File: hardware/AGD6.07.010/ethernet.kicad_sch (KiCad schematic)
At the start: 0 parts

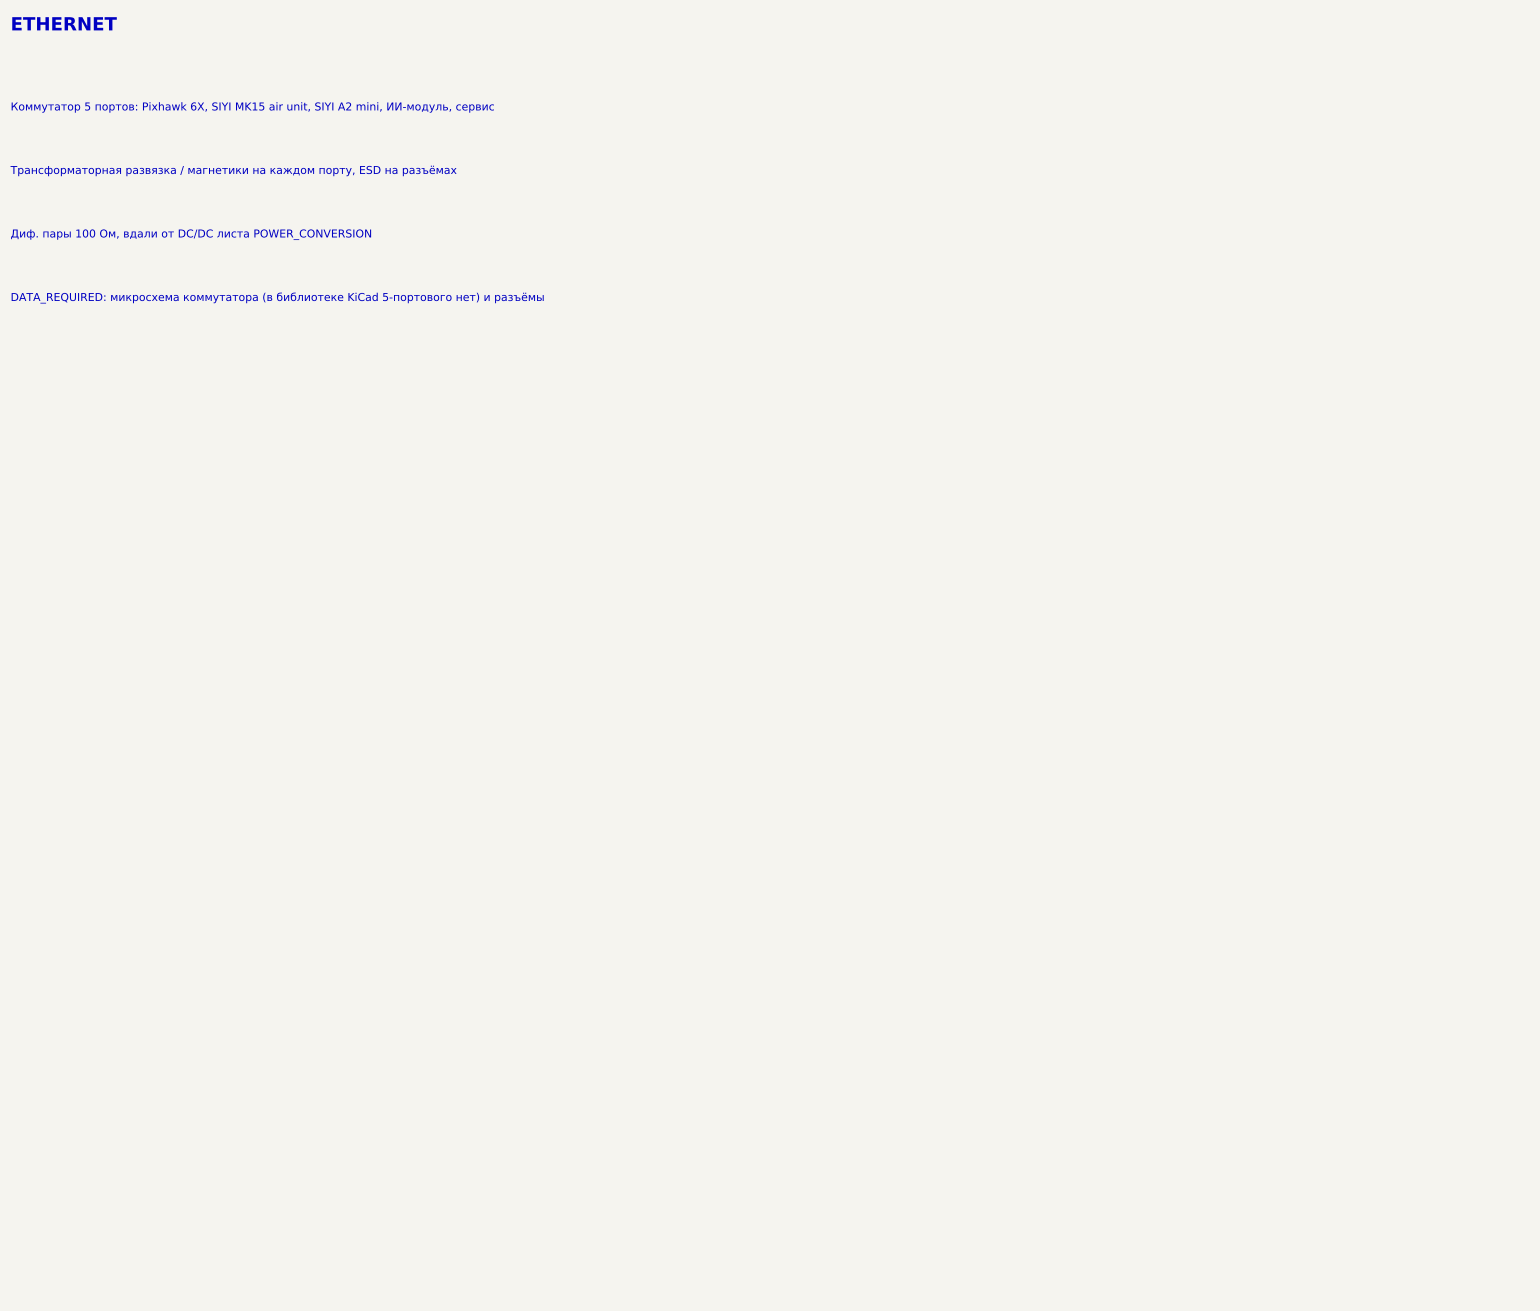
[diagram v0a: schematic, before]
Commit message: Draw full AGD6.07.010 schematic per integrated_avionics_board spec
All ten sheets now carry components: 14S input with hot-swap and power
monitor, 12/5/3.3 V rails and a separate 12 V AI channel with soft-start
and current telemetry, Pixhawk connectors, CAN1/CAN2 hub with chokes,
ESD and switchable termination, sensor conditioning, SIYI and radar,
AI interface and watchdog, protected 12 V switches with diagnostics,
fan/heater control, cameras and Ethernet. Open choices are recorded in
DECISIONS.md; datasheet-dependent values are flagged CHECK_DATASHEET.

ERC: no errors. All 752 intended pin connections match the KiCad netlist.

Co-Authored-By: Claude Opus 5.5 <noreply@anthropic.com>
Claude-Session: https://claude.ai/code/session_01Qk7uTKdi6YbndB9fGuguYV
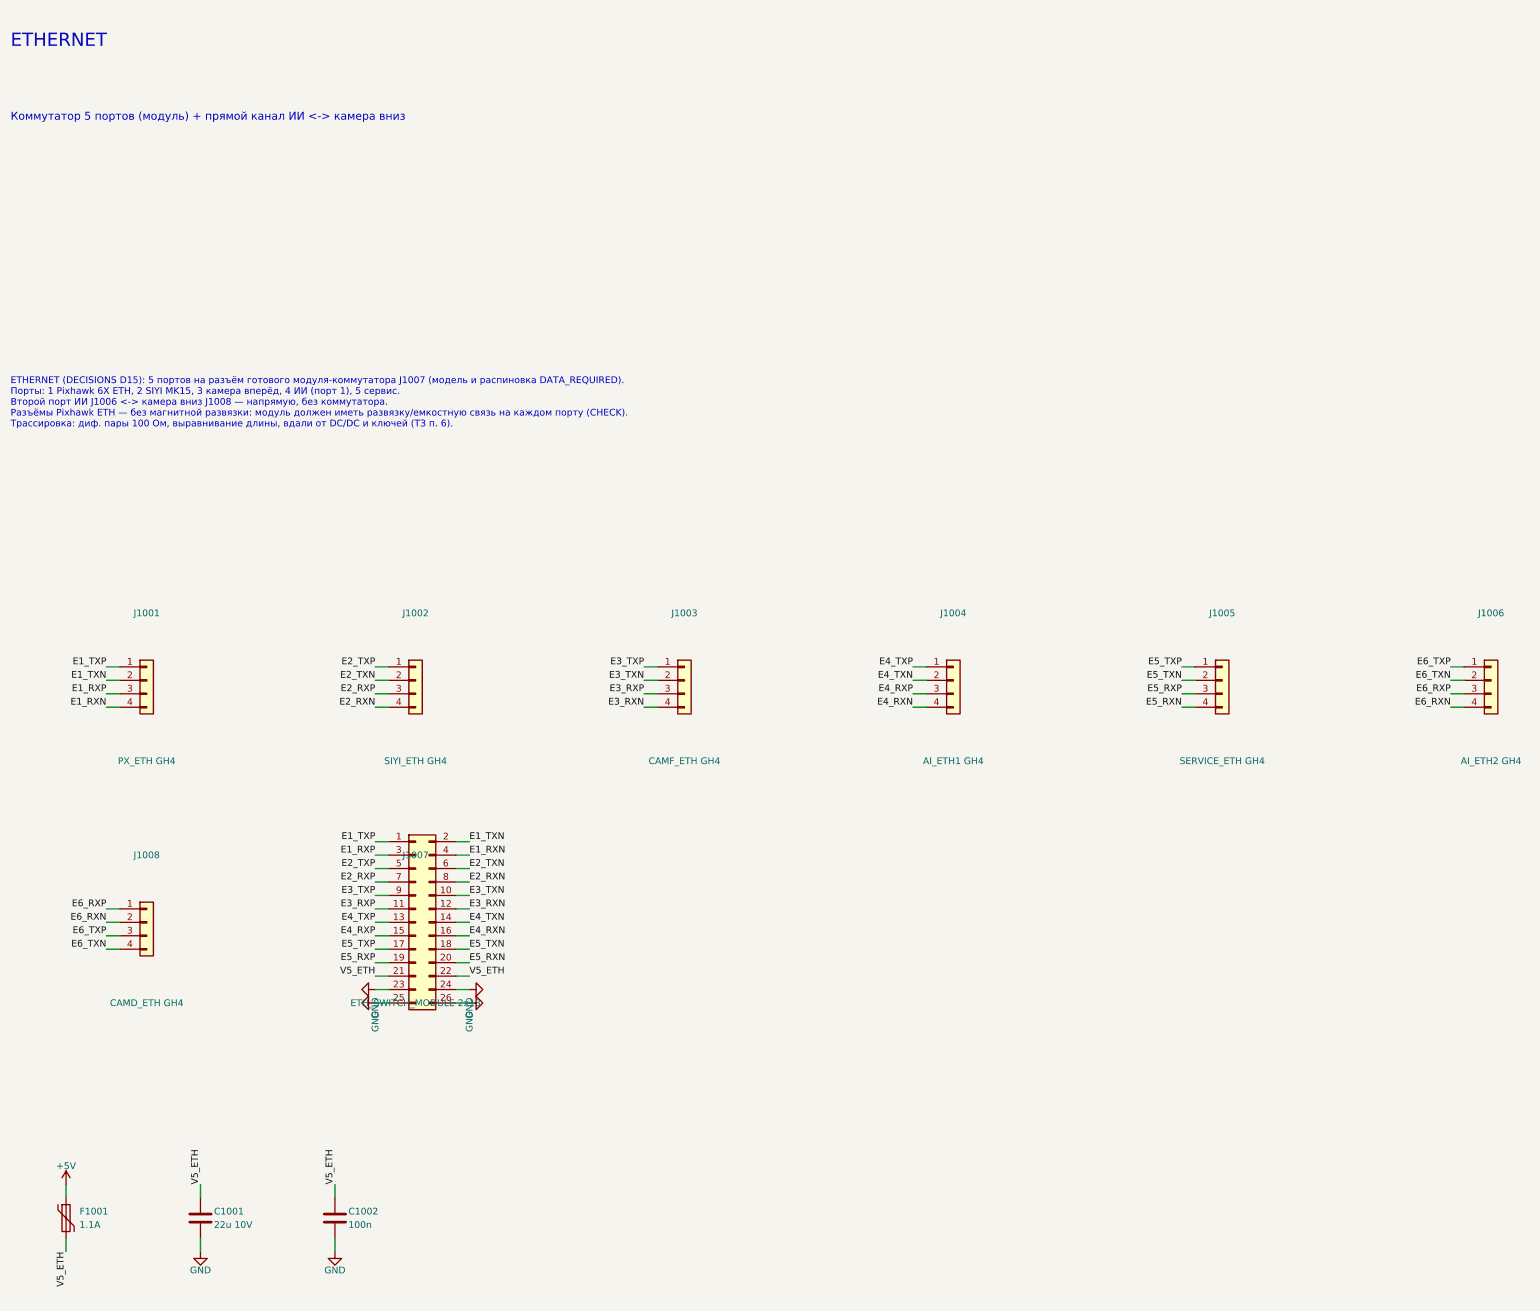
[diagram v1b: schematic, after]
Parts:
- added C1001: 22u 10V, Capacitor_SMD:C_0805_2012Metric, symbol Device:C
- added C1002: 100n, Capacitor_SMD:C_0402_1005Metric, symbol Device:C
- added F1001: 1.1A, Fuse:Fuse_1812_4532Metric, symbol Device:Polyfuse
- added J1001: PX_ETH GH4, Connector_JST:JST_GH_SM04B-GHS-TB_1x04-1MP_P1.25mm_Horizontal, symbol Connector_Generic:Conn_01x04
- added J1002: SIYI_ETH GH4, Connector_JST:JST_GH_SM04B-GHS-TB_1x04-1MP_P1.25mm_Horizontal, symbol Connector_Generic:Conn_01x04
- added J1003: CAMF_ETH GH4, Connector_JST:JST_GH_SM04B-GHS-TB_1x04-1MP_P1.25mm_Horizontal, symbol Connector_Generic:Conn_01x04
- added J1004: AI_ETH1 GH4, Connector_JST:JST_GH_SM04B-GHS-TB_1x04-1MP_P1.25mm_Horizontal, symbol Connector_Generic:Conn_01x04
- added J1005: SERVICE_ETH GH4, Connector_JST:JST_GH_SM04B-GHS-TB_1x04-1MP_P1.25mm_Horizontal, symbol Connector_Generic:Conn_01x04
- added J1006: AI_ETH2 GH4, Connector_JST:JST_GH_SM04B-GHS-TB_1x04-1MP_P1.25mm_Horizontal, symbol Connector_Generic:Conn_01x04
- added J1007: ETH_SWITCH_MODULE 2x13, Connector_PinHeader_2.54mm:PinHeader_2x13_P2.54mm_Vertical, symbol Connector_Generic:Conn_02x13_Odd_Even
- added J1008: CAMD_ETH GH4, Connector_JST:JST_GH_SM04B-GHS-TB_1x04-1MP_P1.25mm_Horizontal, symbol Connector_Generic:Conn_01x04
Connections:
- new net +5V: F1001.1
- new net E1_RXN: J1001.4 (Pin_4), J1007.4 (Pin_4)
- new net E1_RXP: J1001.3 (Pin_3), J1007.3 (Pin_3)
- new net E1_TXN: J1001.2 (Pin_2), J1007.2 (Pin_2)
- new net E1_TXP: J1001.1 (Pin_1), J1007.1 (Pin_1)
- new net E2_RXN: J1002.4 (Pin_4), J1007.8 (Pin_8)
- new net E2_RXP: J1002.3 (Pin_3), J1007.7 (Pin_7)
- new net E2_TXN: J1002.2 (Pin_2), J1007.6 (Pin_6)
- new net E2_TXP: J1002.1 (Pin_1), J1007.5 (Pin_5)
- new net E3_RXN: J1003.4 (Pin_4), J1007.12 (Pin_12)
- new net E3_RXP: J1003.3 (Pin_3), J1007.11 (Pin_11)
- new net E3_TXN: J1003.2 (Pin_2), J1007.10 (Pin_10)
- new net E3_TXP: J1003.1 (Pin_1), J1007.9 (Pin_9)
- new net E4_RXN: J1004.4 (Pin_4), J1007.16 (Pin_16)
- new net E4_RXP: J1004.3 (Pin_3), J1007.15 (Pin_15)
- new net E4_TXN: J1004.2 (Pin_2), J1007.14 (Pin_14)
- new net E4_TXP: J1004.1 (Pin_1), J1007.13 (Pin_13)
- new net E5_RXN: J1005.4 (Pin_4), J1007.20 (Pin_20)
- new net E5_RXP: J1005.3 (Pin_3), J1007.19 (Pin_19)
- new net E5_TXN: J1005.2 (Pin_2), J1007.18 (Pin_18)
- new net E5_TXP: J1005.1 (Pin_1), J1007.17 (Pin_17)
- new net E6_RXN: J1006.4 (Pin_4), J1008.2 (Pin_2)
- new net E6_RXP: J1006.3 (Pin_3), J1008.1 (Pin_1)
- new net E6_TXN: J1006.2 (Pin_2), J1008.4 (Pin_4)
- new net E6_TXP: J1006.1 (Pin_1), J1008.3 (Pin_3)
- new net GND: C1001.2, C1002.2, J1007.23 (Pin_23), J1007.24 (Pin_24), J1007.25 (Pin_25), J1007.26 (Pin_26)
- new net V5_ETH: C1001.1, C1002.1, F1001.2, J1007.21 (Pin_21), J1007.22 (Pin_22)
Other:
- note added: "ETHERNET (DECISIONS D15): 5 портов на разъём готового модуля-коммутатора J1007 (модель и распиновка DATA_REQUIRED). Порты: 1 Pixhawk 6X ETH, 2 SIYI MK15, 3 камера вперёд, 4 ИИ (порт 1), 5 сервис. Второй порт ИИ J1006 <-> камера вниз J1008 — напрямую, без коммутатора. Разъёмы Pixhawk ETH — без магнитной развязки: модуль должен иметь развязку/емкостную связь на каждом порту (CHECK). Трассировка: ди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"
- note added: "Коммутатор 5 портов (модуль) + прямой канал ИИ <-> камера вниз"
- note removed: "DATA_REQUIRED: микросхема коммутатора (в библиотеке KiCad 5-портового нет) и разъёмы"
- note removed: "Диф. пары 100 Ом, вдали от DC/DC листа POWER_CONVERSION"
- note removed: "Коммутатор 5 портов: Pixhawk 6X, SIYI MK15 air unit, SIYI A2 mini, ИИ-модуль, сервис"
- note removed: "Трансформаторная развязка / магнетики на каждом порту, ESD на разъёмах"
- company: (none) -> АГД6.07.010
- title: (none) -> ETHERNET
